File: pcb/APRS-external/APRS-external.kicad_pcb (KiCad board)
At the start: 2 copper layers, 68 x 48 mm, 26 parts, among them J2 To-Radio, J3 Ext Power, J4 GPS, Q1 2N2222, U1 L7805

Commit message: updated boards
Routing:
- net /GPS_RX: track 104.0 -> 96.5 mm
- net Net-(D1-K): track 118.7 -> 113.7 mm
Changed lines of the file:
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@@
 		(allow_soldermask_bridges_in_footprints no)
 		(pcbplotparams
-			(layerselection 0x00010fc_ffffffff)
+			(layerselection 0x0001000_ffffffff)
 			(plot_on_all_layers_selection 0x0000000_00000000)
 			(disableapertmacros no)
@@
 			(outputformat 1)
 			(mirror no)
-			(drillshape 1)
+			(drillshape 0)
 			(scaleselection 1)
-			(outputdirectory "")
+			(outputdirectory "out/")
 		)
 	)
@@
 		(tags "LED diameter 5.0mm 2 pins")
 		(property "Reference" "D3"
-			(at 1.27 3.96 360)
+			(at 1.27 3.96 0)
 			(layer "B.SilkS")
 			(effects
@@
 		)
 		(property "Value" "LED"
-			(at 1.27 -3.96 360)
+			(at 1.27 -3.96 0)
 			(layer "B.Fab")
 			(effects
@@
 		)
 		(fp_text user "${REFERENCE}"
-			(at 0 0 360)
+			(at 0 0 0)
 			(layer "B.Fab")
 			(effects
@@
 		(tags "LED diameter 5.0mm 2 pins")
 		(property "Reference" "D2"
-			(at 1.27 3.96 360)
+			(at 1.27 3.96 0)
 			(layer "B.SilkS")
 			(effects
@@
 		)
 		(property "Value" "LED"
-			(at 1.27 -3.96 360)
+			(at 1.27 -3.96 0)
 			(layer "B.Fab")
 			(effects
@@
 		)
 		(fp_text user "${REFERENCE}"
-			(at 1.25 0 360)
+			(at 1.25 0 0)
 			(layer "B.Fab")
 			(effects
@@
 	)
 	(segment
-		(start 42.5 82.846576)
-		(end 42.5 82.25)
-		(width 0.508)
-		(layer "F.Cu")
-		(net 12)
-	)
-	(segment
-		(start 42.5 82.25)
-		(end 36.792 76.542)
+		(start 56 45.5)
+		(end 56 48.75)
 		(width 0.508)
 		(layer "F.Cu")
@@
 	)
 	(segment
-		(start 36.792 76.542)
-		(end 36.792 71.4)
+		(start 42.5 82.846576)
+		(end 42.5 82.25)
 		(width 0.508)
 		(layer "F.Cu")
@@
 	)
 	(segment
-		(start 39.246 59.496)
-		(end 42.75 63)
+		(start 42.75 63)
+		(end 39.246 59.496)
 		(width 0.508)
 		(layer "F.Cu")
@@
 	)
 	(segment
-		(start 41.106576 44)
-		(end 39.246 45.860576)
+		(start 56 48.75)
+		(end 59.83 52.58)
 		(width 0.508)
 		(layer "F.Cu")
@@
 	)
 	(segment
-		(start 58 44)
-		(end 41.106576 44)
+		(start 42.75 85.5)
+		(end 42.75 83.096576)
 		(width 0.508)
 		(layer "F.Cu")
@@
 	)
 	(segment
-		(start 62 51.5)
-		(end 62 48)
+		(start 39.246 59.496)
+		(end 39.246 45.860576)
 		(width 0.508)
 		(layer "F.Cu")
@@
 	)
 	(segment
-		(start 36.792 71.4)
-		(end 42.096 66.096)
+		(start 36.792 76.542)
+		(end 36.792 71.4)
 		(width 0.508)
 		(layer "F.Cu")
@@
 	)
 	(segment
-		(start 42.75 65.442)
-		(end 42.096 66.096)
+		(start 36.792 71.4)
+		(end 42.75 65.442)
 		(width 0.508)
 		(layer "F.Cu")
@@
 	)
 	(segment
-		(start 42.75 63)
-		(end 42.75 65.442)
+		(start 54.5 44)
+		(end 56 45.5)
 		(width 0.508)
 		(layer "F.Cu")
@@
 	)
 	(segment
-		(start 42.75 85.5)
-		(end 42.75 83.096576)
+		(start 39.246 45.860576)
+		(end 41.106576 44)
 		(width 0.508)
 		(layer "F.Cu")
@@
 	)
 	(segment
-		(start 63.08 52.58)
-		(end 62 51.5)
+		(start 42.75 65.442)
+		(end 42.75 63)
 		(width 0.508)
 		(layer "F.Cu")
@@
 	)
 	(segment
-		(start 67 52.58)
-		(end 63.08 52.58)
+		(start 41.106576 44)
+		(end 54.5 44)
 		(width 0.508)
 		(layer "F.Cu")
@@
 	)
 	(segment
-		(start 62 48)
-		(end 58 44)
+		(start 42.5 82.25)
+		(end 36.792 76.542)
 		(width 0.508)
 		(layer "F.Cu")
@@
 	)
 	(segment
-		(start 39.246 45.860576)
-		(end 39.246 59.496)
+		(start 59.83 52.58)
+		(end 67 52.58)
 		(width 0.508)
 		(layer "F.Cu")
@@
 	)
 	(segment
-		(start 80.424 86.040135)
-		(end 80.424 83.460576)
+		(start 80.424 83.460576)
+		(end 77.209424 80.246)
 		(width 0.508)
 		(layer "F.Cu")
@@
 	)
 	(segment
-		(start 70.479259 47.327317)
-		(end 68.056576 49.75)
+		(start 77.209424 53.29184)
+		(end 79.124 51.377264)
 		(width 0.508)
 		(layer "F.Cu")
@@
 	)
 	(segment
-		(start 42.21 87.5)
-		(end 78.964135 87.5)
+		(start 80.424 86.040135)
+		(end 80.424 83.460576)
 		(width 0.508)
 		(layer "F.Cu")
@@
 	)
 	(segment
-		(start 68.056576 49.75)
-		(end 63.25 49.75)
+		(start 78.964135 87.5)
+		(end 80.424 86.040135)
 		(width 0.508)
 		(layer "F.Cu")
@@
 	)
 	(segment
-		(start 75.876 47.327317)
-		(end 70.479259 47.327317)
+		(start 40.21 85.5)
+		(end 42.21 87.5)
 		(width 0.508)
 		(layer "F.Cu")
@@
 	)
 	(segment
-		(start 79.124 51.377264)
-		(end 79.124 47.327317)
+		(start 67.766576 50.04)
+		(end 67 50.04)
 		(width 0.508)
 		(layer "F.Cu")
@@
 	)
 	(segment
-		(start 77.209424 53.29184)
-		(end 79.124 51.377264)
+		(start 79.124 51.377264)
+		(end 79.124 47.327317)
 		(width 0.508)
 		(layer "F.Cu")
@@
 	)
 	(segment
-		(start 79.124 47.327317)
-		(end 78.172683 46.376)
-		(width 0.508)
-		(layer "F.Cu")
-		(net 22)
-	)
-	(segment
-		(start 63.54 50.04)
-		(end 67 50.04)
+		(start 75.876 47.327317)
+		(end 70.479259 47.327317)
 		(width 0.508)
 		(layer "F.Cu")
@@
 	)
 	(segment
-		(start 40.21 85.5)
-		(end 42.21 87.5)
+		(start 42.21 87.5)
+		(end 78.964135 87.5)
 		(width 0.508)
 		(layer "F.Cu")
@@
 	)
 	(segment
-		(start 77.209424 80.246)
-		(end 77.209424 53.29184)
+		(start 70.479259 47.327317)
+		(end 67.766576 50.04)
 		(width 0.508)
 		(layer "F.Cu")
@@
 	)
 	(segment
-		(start 78.964135 87.5)
-		(end 80.424 86.040135)
+		(start 79.124 47.327317)
+		(end 78.172683 46.376)
 		(width 0.508)
 		(layer "F.Cu")
@@
 	)
 	(segment
-		(start 63.25 49.75)
-		(end 63.54 50.04)
-		(width 0.508)
-		(layer "F.Cu")
-		(net 22)
-	)
-	(segment
-		(start 80.424 83.460576)
-		(end 77.209424 80.246)
+		(start 77.209424 80.246)
+		(end 77.209424 53.29184)
 		(width 0.508)
 		(layer "F.Cu")
@@
 	(segment
 		(start 39.184 43.066)
-		(end 60.566 43.066)
+		(end 36.5 45.75)
 		(width 0.508)
 		(layer "B.Cu")
@@
 	)
 	(segment
-		(start 36.5 45.75)
+		(start 52.066 43.066)
 		(end 39.184 43.066)
 		(width 0.508)
@@
 	)
 	(segment
-		(start 60.566 43.066)
-		(end 62.04 44.54)
+		(start 36.5 59.25)
+		(end 34.75 61)
 		(width 0.508)
 		(layer "B.Cu")
@@
 	)
 	(segment
-		(start 43.25 68.5)
-		(end 48.75 74)
+		(start 62.04 53.04)
+		(end 52.066 43.066)
 		(width 0.508)
 		(layer "B.Cu")
@@
 	)
 	(segment
-		(start 51.25 86.25)
-		(end 56.25 86.25)
+		(start 34.75 61)
+		(end 29.5 61)
 		(width 0.508)
 		(layer "B.Cu")
@@
 	)
 	(segment
-		(start 36.5 59.25)
-		(end 36.5 45.75)
+		(start 43.25 68.5)
+		(end 48.75 74)
 		(width 0.508)
 		(layer "B.Cu")
@@
 	)
 	(segment
-		(start 34.75 61)
-		(end 36.5 59.25)
+		(start 51.25 86.25)
+		(end 56.25 86.25)
 		(width 0.508)
 		(layer "B.Cu")
@@
 	)
 	(segment
-		(start 62.04 80.46)
-		(end 62.04 61.98)
+		(start 62.04 61.98)
+		(end 62.04 53.04)
 		(width 0.508)
 		(layer "B.Cu")
@@
 	)
 	(segment
-		(start 48.75 74)
-		(end 48.75 83.75)
+		(start 36.5 45.75)
+		(end 36.5 59.25)
 		(width 0.508)
 		(layer "B.Cu")
@@
 	)
 	(segment
-		(start 29.5 61)
-		(end 34.75 61)
+		(start 62.04 80.46)
+		(end 62.04 61.98)
 		(width 0.508)
 		(layer "B.Cu")
@@
 	)
 	(segment
-		(start 62.04 44.54)
-		(end 62.04 61.98)
+		(start 48.75 74)
+		(end 48.75 83.75)
 		(width 0.508)
 		(layer "B.Cu")

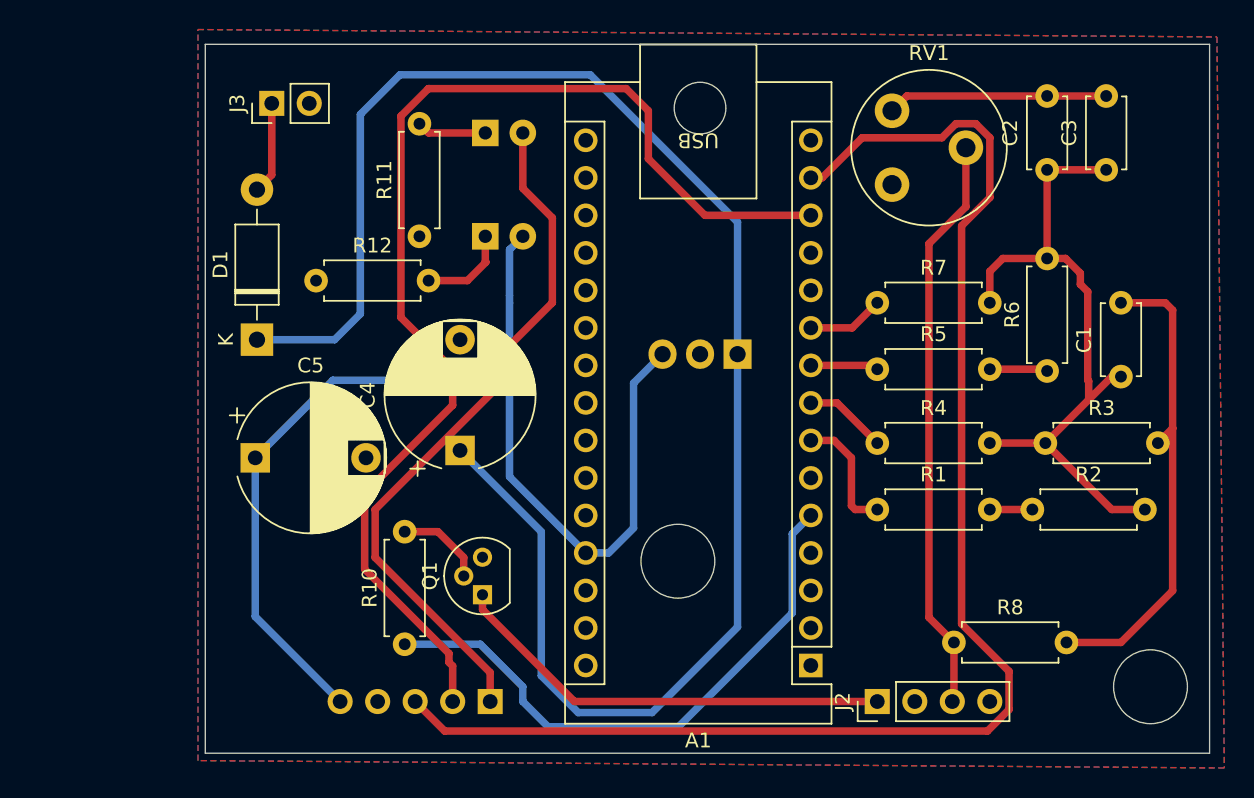
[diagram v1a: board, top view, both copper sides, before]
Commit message: added fixes for physical constraints on the GPS
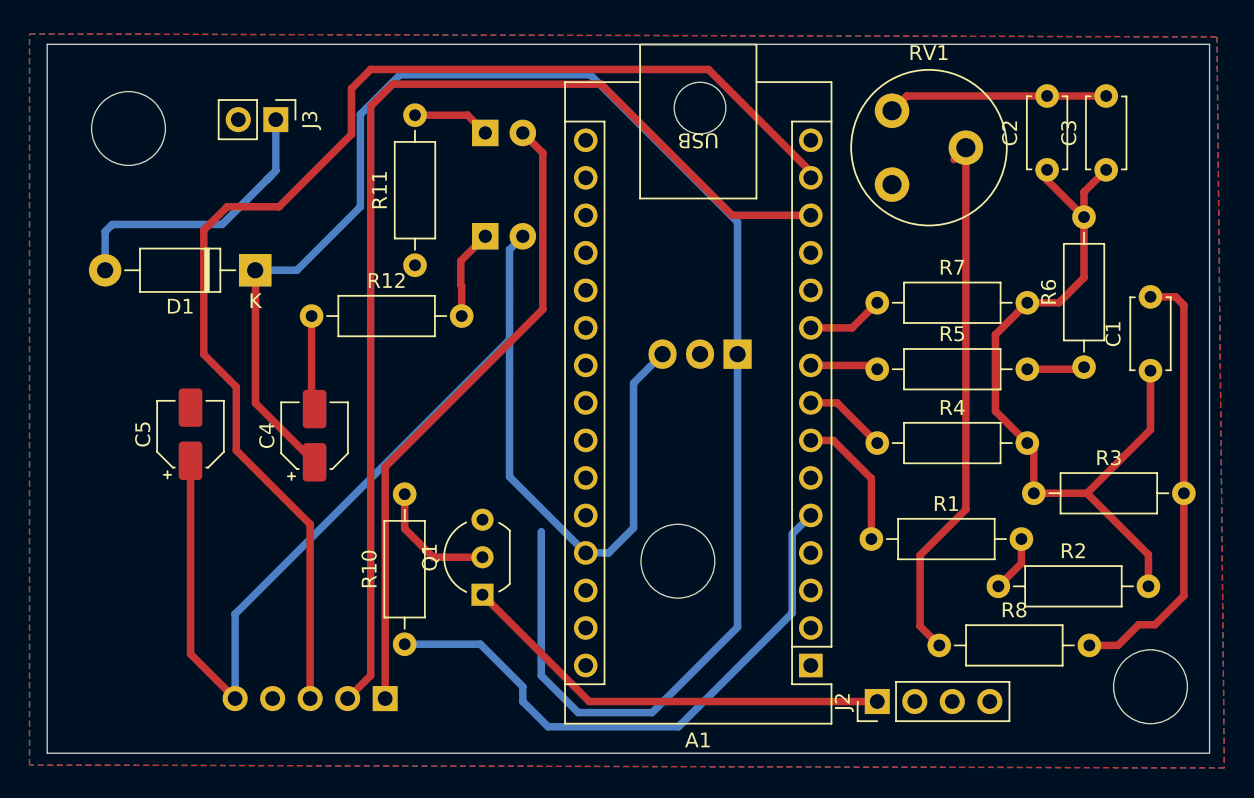
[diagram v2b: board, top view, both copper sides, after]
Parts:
- C4, C5: footprint Capacitor_THT:CP_Radial_D10.0mm_P7.50mm -> Capacitor_SMD:CP_Elec_4x4.5
- Q1: footprint Package_TO_SOT_THT:TO-92 -> Package_TO_SOT_THT:TO-92_Inline_Wide
- R1, R10, R11, R12, R2, R3, R4, R5, R6, R7, R8: footprint Resistor_THT:R_Axial_DIN0207_L6.3mm_D2.5mm_P7.62mm_Horizontal -> Resistor_THT:R_Axial_DIN0207_L6.3mm_D2.5mm_P10.16mm_Horizontal
- moved C4 9.90 mm to (33.4, 67.5)
- moved J4 7.11 mm to (38.2, 85.3)
- moved R2 5.69 mm to (79.7, 77.7)
- moved D1 4.70 mm to (29.4, 56.3), turned to 180 degrees
- moved C5 4.67 mm to (25.0, 67.4), turned to 90 degrees
- moved R3 3.49 mm to (82.1, 71.4)
- moved R6 2.51 mm to (85.5, 62.9)
- moved R12 2.42 mm to (33.2, 59.4)
- moved R1 2.04 mm to (71.1, 74.5)
- moved C1 2.04 mm to (90.0, 63.1)
- moved R11 1.98 mm to (40.2, 56.0)
- moved J3 1.13 mm to (30.8, 46.1), turned to -90 degrees
- moved R8 1.01 mm to (75.7, 81.7)
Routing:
- net Net-(D1-A): track 6.25 -> 19.8 mm
- net /GPS_RX: track 96.5 -> 85.4 mm
- net VCC: track 79.9 -> 89.8 mm
- net GND: track 0.00 -> 6.38 mm
- net Net-(C1-Pad1): track 47.2 -> 53.3 mm
- net /GPS_TX: track 80.0 -> 74.8 mm
- net /PPS: track 47.5 -> 43.3 mm
- net Net-(C1-Pad2): track 32.8 -> 30.0 mm
- net /Audio_in: track 39.3 -> 36.7 mm
- net Net-(Q1-B): track 5.97 -> 8.41 mm
- net Net-(D1-K): track 113.7 -> 114.7 mm
- net Net-(R1-Pad2): track 2.88 -> 3.85 mm
- net Net-(A1-D4): track 8.34 -> 9.27 mm
- net /PTT: track 30.3 -> 29.7 mm
- net Net-(D2-K): track 4.72 -> 5.26 mm
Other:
- board size 68 x 48 mm -> 78.7 x 48 mm

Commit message: updated silk screen print locations
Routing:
- net /Audio_in: track 36.7 -> 40.8 mm
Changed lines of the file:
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@@
 		(tags "Resistor Axial_DIN0207 series Axial Horizontal pin pitch 10.16mm 0.25W = 1/4W length 6.3mm diameter 2.5mm")
 		(property "Reference" "R8"
-			(at 5.08 -2.37 0)
+			(at 8 2.2 0)
 			(layer "F.SilkS")
 			(effects
@@
 		(tags "Potentiometer vertical Piher PT-10-V05")
 		(property "Reference" "RV1"
-			(at 2.5 -8.9 0)
+			(at 1 4 180)
 			(layer "F.SilkS")
 			(effects
@@
 		(tags "C Disc series Radial pin pitch 5.00mm  diameter 4.7mm width 2.5mm Capacitor")
 		(property "Reference" "C2"
-			(at 2.5 -2.5 90)
+			(at -2.3 -0.3 180)
 			(layer "F.SilkS")
 			(effects
@@
 		)
 		(fp_text user "${REFERENCE}"
-			(at -3.5 5.04 360)
+			(at -3.5 5.04 0)
 			(layer "F.Fab")
 			(effects
@@
 		(tags "C Disc series Radial pin pitch 5.00mm  diameter 4.7mm width 2.5mm Capacitor")
 		(property "Reference" "C3"
-			(at 2.5 -2.5 90)
+			(at 2.4 2.4 -90)
 			(layer "F.SilkS")
 			(effects
@@
 		(tags "Diode DO-41_SOD81 series Axial Horizontal pin pitch 10.16mm  length 5.2mm diameter 2.7mm")
 		(property "Reference" "D1"
-			(at 5.08 -2.47 360)
+			(at 5.08 -2.47 0)
 			(layer "F.SilkS")
 			(effects
@@
 		)
 		(property "Value" "1N4001"
-			(at 5.08 2.47 360)
+			(at 5.08 2.47 0)
 			(layer "F.Fab")
 			(effects
@@
 		)
 		(fp_text user "K"
-			(at 0 -2.1 360)
+			(at 0 -2.1 0)
 			(layer "F.SilkS")
 			(effects
@@
 		)
 		(fp_text user "K"
-			(at 0 -2.1 360)
+			(at 0 -2.1 0)
 			(layer "F.Fab")
 			(effects
@@
 		)
 		(fp_text user "${REFERENCE}"
-			(at 5.3 -5.2 360)
+			(at 5.3 -5.2 0)
 			(layer "F.Fab")
 			(effects
@@
 		(tags "C Disc series Radial pin pitch 5.00mm  diameter 4.7mm width 2.5mm Capacitor")
 		(property "Reference" "C1"
-			(at 2.5 -2.5 90)
+			(at 6.9 0 180)
 			(layer "F.SilkS")
 			(effects
@@
 		(tags "to-92 sc-43 sc-43a sot54 PA33 transistor")
 		(property "Reference" "Q1"
-			(at 2.54 -3.56 90)
+			(at 7.17 -0.27 180)
 			(layer "F.SilkS")
 			(effects
@@
 		(tags "Resistor Axial_DIN0207 series Axial Horizontal pin pitch 10.16mm 0.25W = 1/4W length 6.3mm diameter 2.5mm")
 		(property "Reference" "R6"
-			(at 5.08 -2.37 90)
+			(at 7.46 -2.2 90)
 			(layer "F.SilkS")
 			(effects
@@
 		(tags "LED diameter 5.0mm 2 pins")
 		(property "Reference" "D3"
-			(at 1.27 3.96 0)
+			(at -2.66 -0.1 -90)
 			(layer "B.SilkS")
 			(effects
@@
 		(tags "LED diameter 5.0mm 2 pins")
 		(property "Reference" "D2"
-			(at 1.27 3.96 0)
+			(at -2.76 0.7 90)
 			(layer "B.SilkS")
 			(effects
@@
 		(tags "TO-220-3 Horizontal RM 2.54mm")
 		(property "Reference" "U1"
-			(at 2.54 20.58 0)
+			(at 3.04 7.58 0)
 			(layer "B.SilkS")
 			(effects
@@
 		)
 		(fp_text user "${REFERENCE}"
-			(at 2.54 20.58 0)
+			(at 3.24 6.28 0)
 			(layer "B.Fab")
 			(effects
@@
 	)
 	(segment
+		(start 76.58 83.32)
+		(end 76.58 85.5)
+		(width 0.508)
+		(layer "F.Cu")
+		(net 38)
+	)
+	(segment
 		(start 74.4 80.4)
 		(end 75.7 81.7)
 		(width 0.508)
 		(layer "F.Cu")
+		(net 38)
+	)
+	(segment
+		(start 75.7 81.7)
+		(end 76.6 82.6)
+		(width 0.508)
+		(layer "F.Cu")
+		(net 38)
+	)
+	(segment
+		(start 76.6 82.6)
+		(end 76.6 83.3)
+		(width 0.508)
+		(layer "F.Cu")
+		(net 38)
+	)
+	(segment
+		(start 76.6 83.3)
+		(end 76.58 83.32)
+		(width 0.508)
+		(layer "F.Cu")

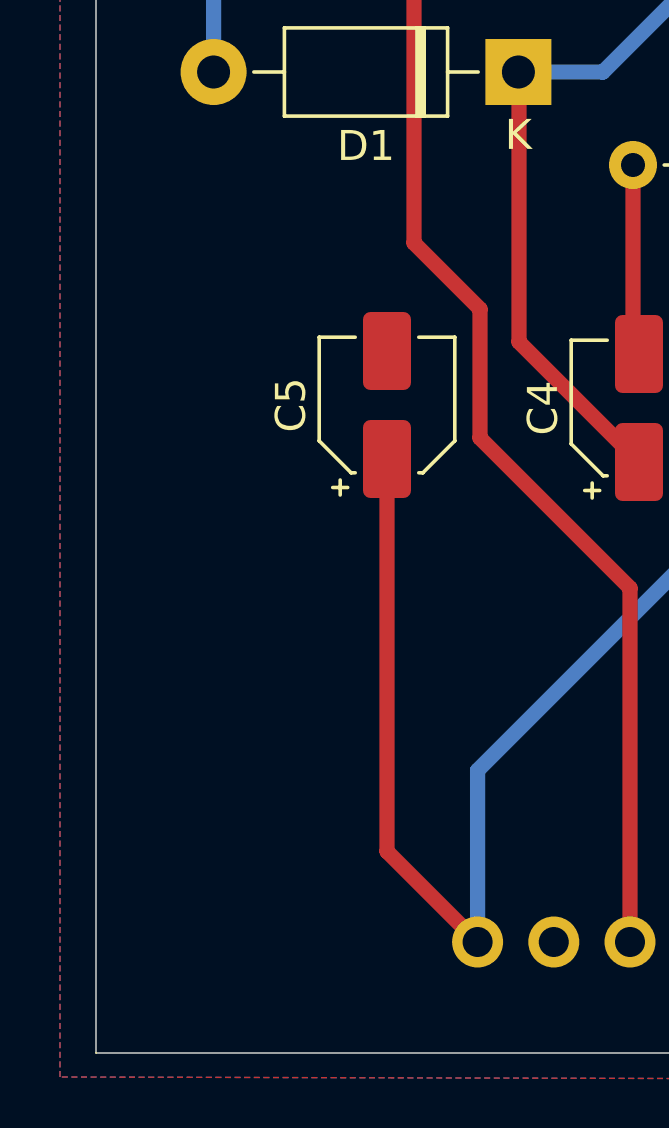
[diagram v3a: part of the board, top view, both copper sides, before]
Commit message: added project label
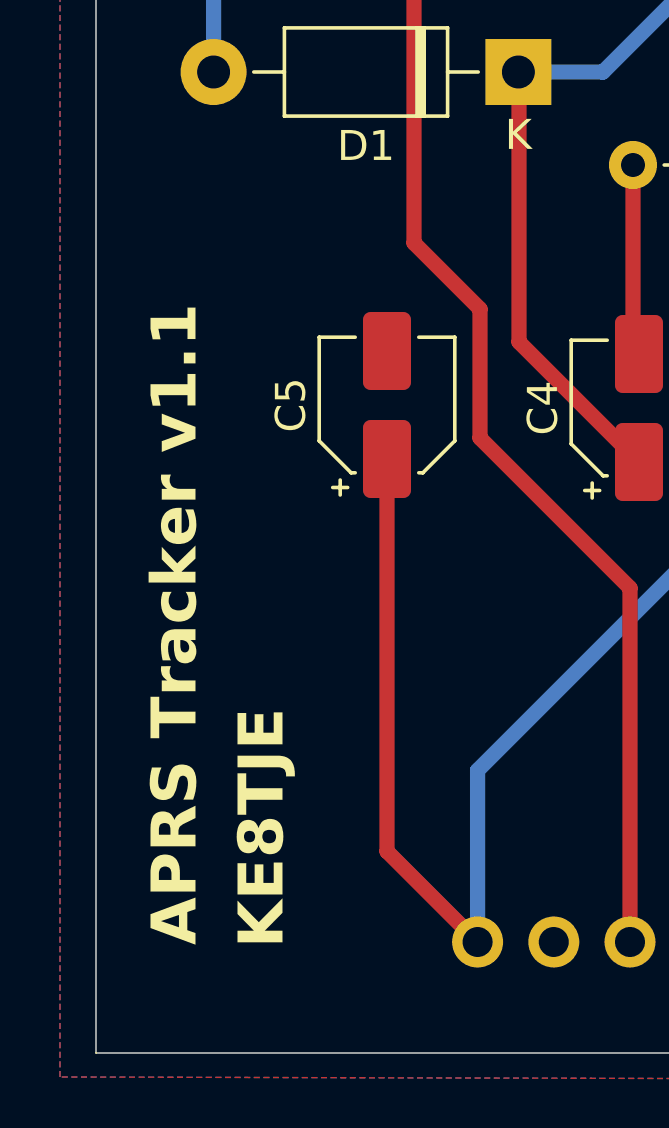
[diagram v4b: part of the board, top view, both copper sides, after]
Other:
- board text added: "APRS Tracker v1.1"
- board text added: "KE8TJE"
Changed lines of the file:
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@@
 		(layer "Edge.Cuts")
+	)
+	(gr_text "KE8TJE"
+		(at 21.7 85.5 90)
+		(layer "F.SilkS")
+		(effects
+			(font
+				(size 1.5 1.5)
+				(thickness 0.3)
+				(bold yes)
+			)
+			(justify left bottom)
+		)
+	)
+	(gr_text "APRS Tracker v1.1"
+		(at 18.8 85.4 90)
+		(layer "F.SilkS")
+		(effects
+			(font
+				(size 1.5 1.5)
+				(thickness 0.3)
+				(bold yes)
+			)
+			(justify left bottom)
+		)
 	)
 	(segment

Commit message: added BOM and final version made with JLC
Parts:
- C1, C2, C3: footprint Capacitor_THT:C_Disc_D4.7mm_W2.5mm_P5.00mm -> Diode_SMD:D_0805_2012Metric_Pad1.15x1.40mm_HandSolder
- moved C1 3.41 mm to (89.7, 66.5), turned to 0 degrees
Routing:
- net Net-(C1-Pad2): track 30.0 -> 21.5 mm
- net Net-(C2-Pad2): track 14.9 -> 22.8 mm
- net Net-(C1-Pad1): track 53.3 -> 50.5 mm
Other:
- outline, holes or cut-outs redrawn
- board text added: "- +"
- board text added: "GND"
- board text added: "PTT"
